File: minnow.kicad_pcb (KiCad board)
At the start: 2 copper layers, 41 x 33 mm, 69 parts, among them J1 USB_C_Receptacle_Host, J3 ARM_JTAG_SWD_10_Male, J4 VCCIO_EXT, J5 PicoBlade, P1 USB_C_Plug, SW1 SW_DIP_x04, U1 FT230XQ, U2 PI5A3157CEX, U3 PI5A3157CEX, U4 USB3740B-AI2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

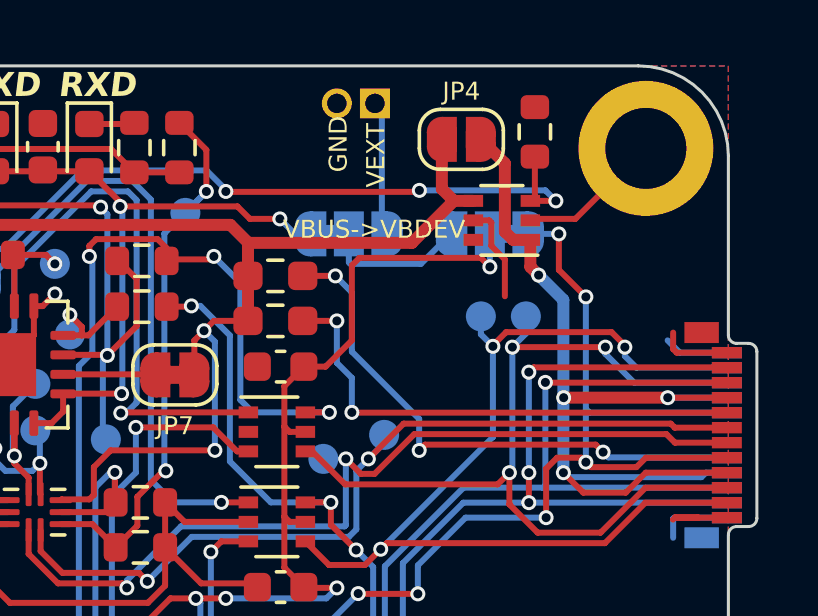
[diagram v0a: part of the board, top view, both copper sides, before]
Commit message: add a white LED for VBUS_DEV
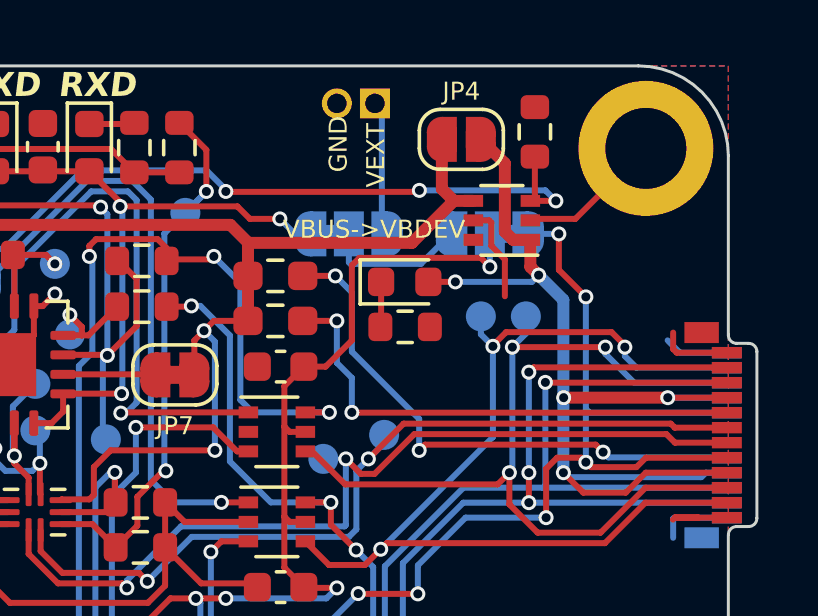
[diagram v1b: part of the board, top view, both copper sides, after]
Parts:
- added D4: WHITE, LED_SMD:LED_0603_1608Metric, F.Cu at (177.2, 45.2)
- added R16: 1k, Resistor_SMD:R_0603_1608Metric, F.Cu at (177.2, 46.7)
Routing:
- net /VBUS_DEV: track 31.6 -> 35.3 mm, vias 4 -> 5
- net Net-(D4-K): track 0.00 -> 1.51 mm

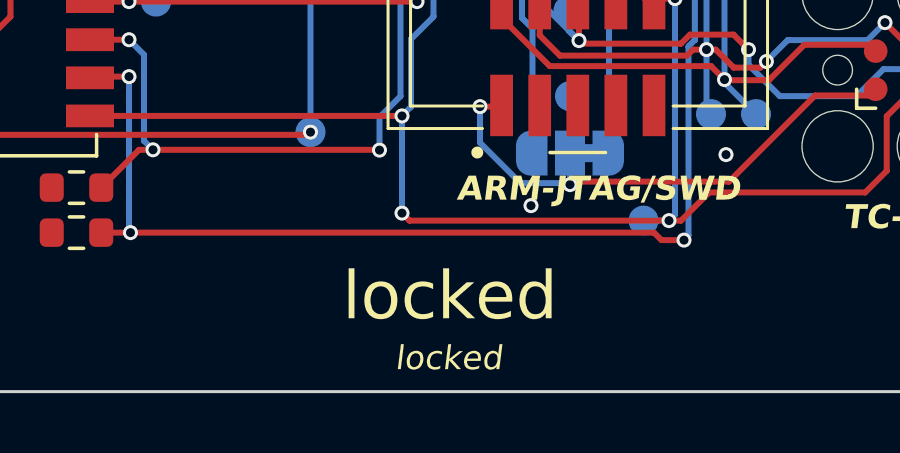
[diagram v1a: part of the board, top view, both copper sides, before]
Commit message: Update Files
Update Files to KiCad 8.0
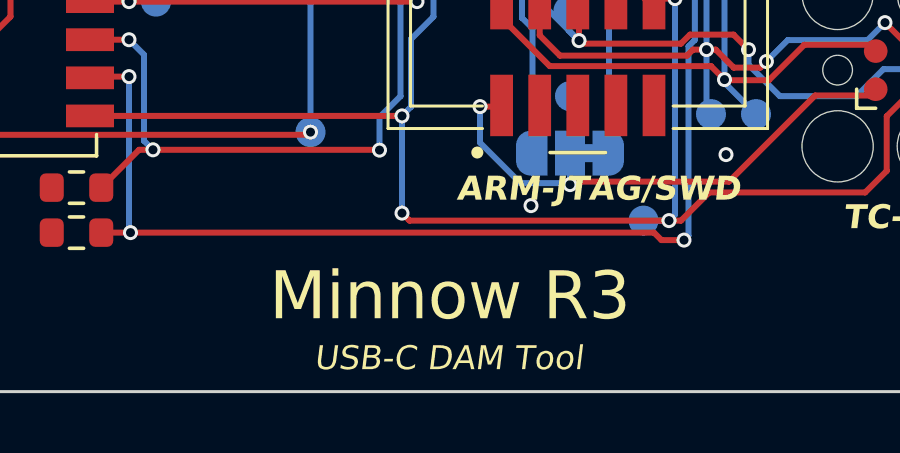
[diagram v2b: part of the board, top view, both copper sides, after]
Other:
- board text added: "Minnow R${REVISION}"
- board text added: "USB-C DAM Tool"
- board text removed: "locked"
